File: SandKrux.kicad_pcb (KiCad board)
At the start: 2 copper layers, 69 parts, among them CN1 527450697, J1 FH12-40S-0.5SH_55_, J2 Connector, USB-TYPE-C-16P, U1 K210_C913414, U2 AXP173, U3 MT9700-N, U4 SGM809-ZXN3L/TR, U4 XC6206P182MR_C347373, U5 GD25LQ128EWIGR, U6 TMI7003C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

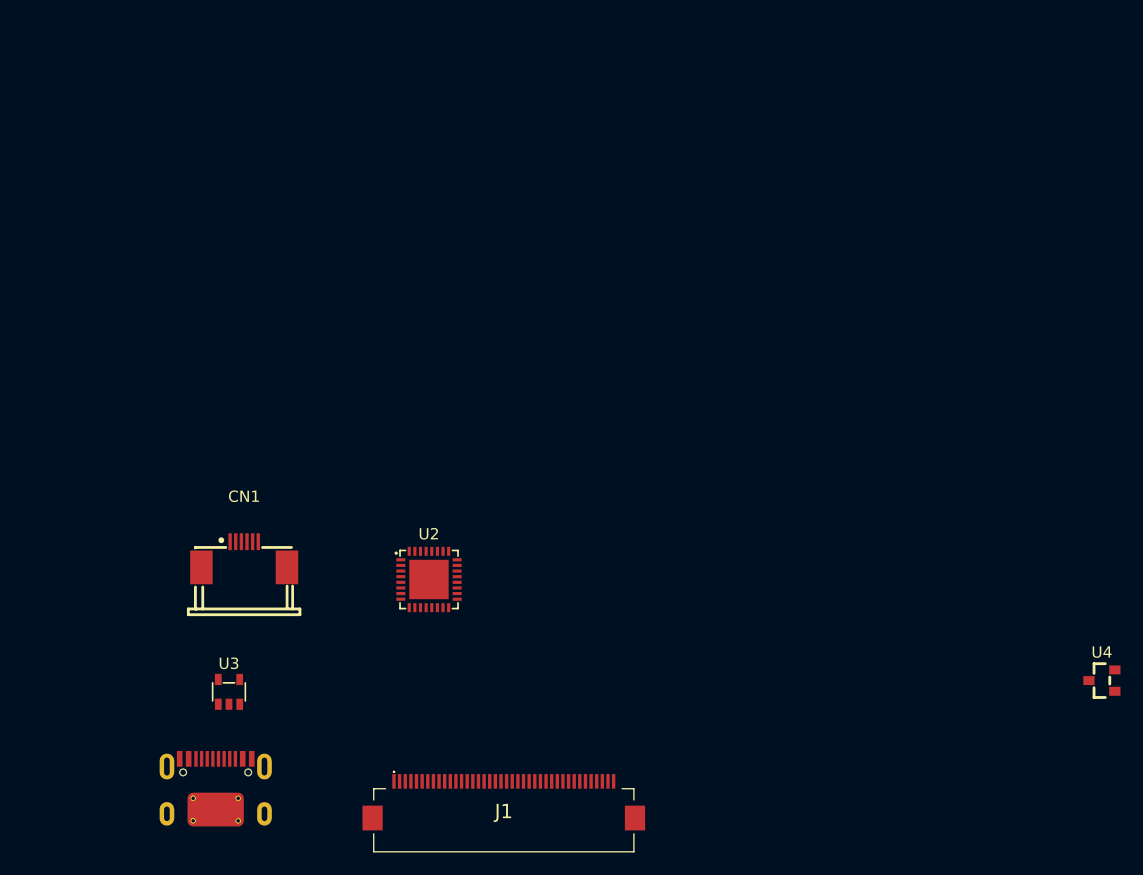
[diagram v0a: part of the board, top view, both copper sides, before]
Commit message: pcb update lcd e toutch
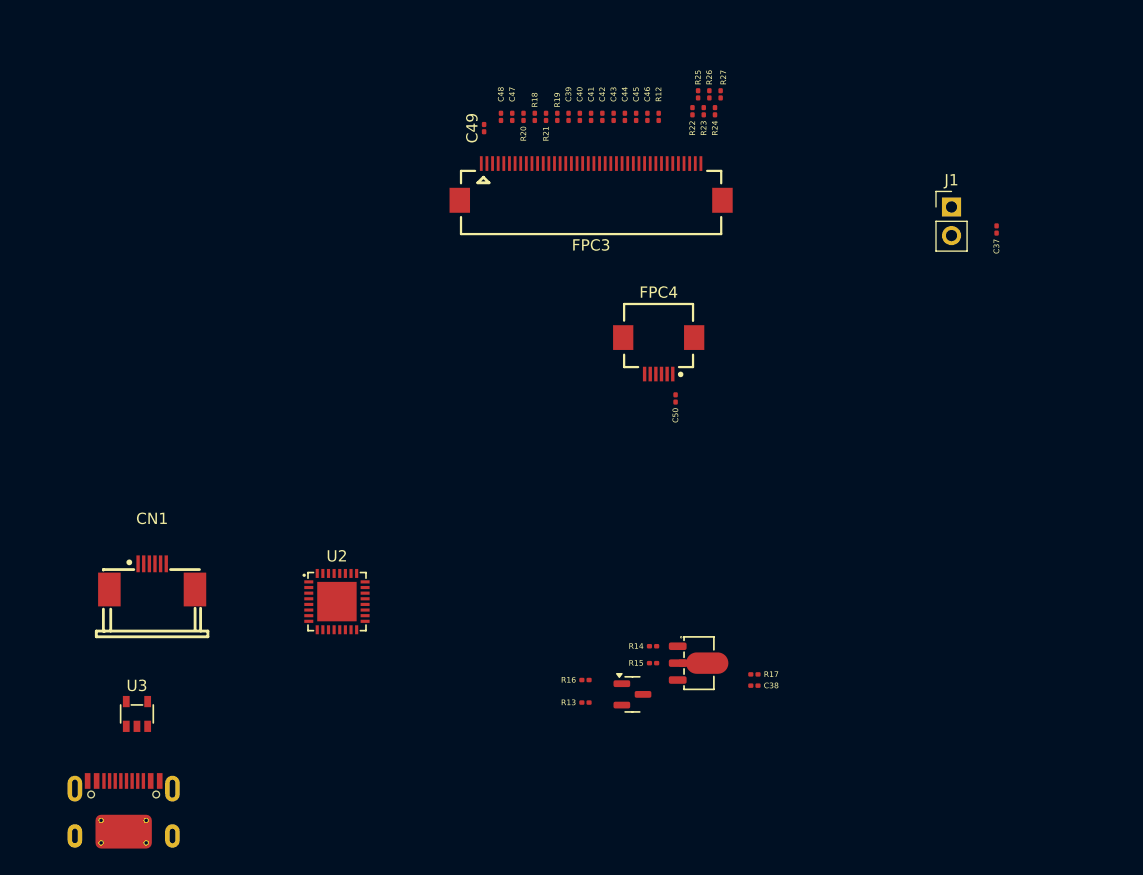
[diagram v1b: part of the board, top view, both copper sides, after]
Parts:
- removed the U4 at (232.8, 90.5)
- added C37: 10uF, Capacitor_SMD:C_0201_0603Metric, F.Cu at (223.5, 50.5)
- added C38: 100nF, Capacitor_SMD:C_0201_0603Metric, F.Cu at (202.0, 91.0)
- added C39: 100pF, Capacitor_SMD:C_0201_0603Metric, F.Cu at (185.5, 40.5)
- added C40: 100pF, Capacitor_SMD:C_0201_0603Metric, F.Cu at (186.5, 40.5)
- added C41: 100pF, Capacitor_SMD:C_0201_0603Metric, F.Cu at (187.5, 40.5)
- added C42: 100pF, Capacitor_SMD:C_0201_0603Metric, F.Cu at (188.5, 40.5)
- added C43: 100pF, Capacitor_SMD:C_0201_0603Metric, F.Cu at (189.5, 40.5)
- added C44: 100pF, Capacitor_SMD:C_0201_0603Metric, F.Cu at (190.5, 40.5)
- added C45: 100pF, Capacitor_SMD:C_0201_0603Metric, F.Cu at (191.5, 40.5)
- added C46: 100pF, Capacitor_SMD:C_0201_0603Metric, F.Cu at (192.5, 40.5)
- added C47: 100pF, Capacitor_SMD:C_0201_0603Metric, F.Cu at (180.5, 40.5)
- added C48: 100pF, Capacitor_SMD:C_0201_0603Metric, F.Cu at (179.5, 40.5)
- added C49: 100nF, Capacitor_SMD:C_0201_0603Metric, F.Cu at (178.0, 41.5)
- added C50: 10uF, Capacitor_SMD:C_0201_0603Metric, F.Cu at (195.0, 65.5)
- added FPC3: FH12-40S-0.5SH(55), easyeda2kicad:FPC-SMD_FH12-40S-0.5SH-55, F.Cu at (187.5, 46.3)
- added FPC4: FH12-6S-0.5SH(55), easyeda2kicad:FPC-SMD_FH12-6S-0.5SH-55, F.Cu at (193.5, 61.7)
- added Q1: S8050, PCM_JLCPCB:Q_SOT-23, F.Cu at (191.2, 91.8)
- added Q2: SI2301CDS-T1-GE3, PCM_JLCPCB:Q_SOT-89, F.Cu at (196.5, 89.0)
- added R12: 5.1R, Resistor_SMD:R_0201_0603Metric, F.Cu at (193.5, 40.5)
- added R13: 100R, Resistor_SMD:R_0201_0603Metric, F.Cu at (187.0, 92.5)
- added R14: 100R, Resistor_SMD:R_0201_0603Metric, F.Cu at (193.0, 87.5)
- added R15: 10K, Resistor_SMD:R_0201_0603Metric, F.Cu at (193.0, 89.0)
- added R16: 10K, Resistor_SMD:R_0201_0603Metric, F.Cu at (187.0, 90.5)
- added R17: 10K, Resistor_SMD:R_0201_0603Metric, F.Cu at (202.0, 90.0)
- added R18: 0R, Resistor_SMD:R_0201_0603Metric, F.Cu at (182.5, 40.5)
- added R19: NC, Resistor_SMD:R_0201_0603Metric, F.Cu at (184.5, 40.5)
- added R20: NC, Resistor_SMD:R_0201_0603Metric, F.Cu at (181.5, 40.5)
- added R21: 0R, Resistor_SMD:R_0201_0603Metric, F.Cu at (183.5, 40.5)
- added R22: NC, Resistor_SMD:R_0201_0603Metric, F.Cu at (196.5, 40.0)
- added R23: NC, Resistor_SMD:R_0201_0603Metric, F.Cu at (197.5, 40.0)
- added R24: 5.1K, Resistor_SMD:R_0201_0603Metric, F.Cu at (198.5, 40.0)
- added R25: 5.1K, Resistor_SMD:R_0201_0603Metric, F.Cu at (197.0, 38.5)
- added R26: 5.1K, Resistor_SMD:R_0201_0603Metric, F.Cu at (198.0, 38.5)
- added R27: NC, Resistor_SMD:R_0201_0603Metric, F.Cu at (199.0, 38.5)
- J1: value FH12-40S-0.5SH_55_ -> Conn_01x02; footprint KiCad:FH1240S05SH55 -> Connector_PinHeader_2.54mm:PinHeader_1x02_P2.54mm_Vertical
- moved J1 66.8 mm to (219.5, 48.5)
- moved CN1 8.40 mm to (148.5, 81.3)
- moved J2 8.40 mm to (146.0, 102.0)
- moved U3 8.40 mm to (147.2, 93.5)
- moved U2 8.40 mm to (164.9, 83.5)
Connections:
- J1 pad 1: unconnected-(J1-Pad1) -> /CAPTOUCH_RST
- J1 pad 2: unconnected-(J1-Pad2) -> /FUNCTION2

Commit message: TFT CARD
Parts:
- added C51: 10uF, Capacitor_SMD:C_0201_0603Metric, F.Cu at (36.0, 61.0)
- added R28: 10K, Resistor_SMD:R_0201_0603Metric, F.Cu at (35.0, 61.0)
- added R29: 10K, Resistor_SMD:R_0201_0603Metric, F.Cu at (39.5, 61.0)
- added U9: HX TF-CARD XG8P H1.5, easyeda2kicad:TF-SMD_HX-TF-CARD-XG8P-H1.5, F.Cu at (36.2, 67.4)

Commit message: usb ports
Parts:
- removed J2: Connector, USB-TYPE-C-16P, PCM_JLCPCB:TYPE-C-SMD_HX-TYPE-C-16PIN
- added R30: 5.1K, Resistor_SMD:R_0201_0603Metric, F.Cu at (81.0, 126.5)
- added R31: 5.1K, Resistor_SMD:R_0201_0603Metric, F.Cu at (84.5, 126.5)
- added R32: 1.5K, Resistor_SMD:R_0201_0603Metric, F.Cu at (63.8, 117.4)
- added R33: 1.5K, Resistor_SMD:R_0201_0603Metric, F.Cu at (63.8, 119.2)
- added R34: 1.5K, Resistor_SMD:R_0201_0603Metric, F.Cu at (66.2, 113.9)
- added R35: 1.5K, Resistor_SMD:R_0201_0603Metric, F.Cu at (66.2, 115.7)
- added R36: 1.5K, Resistor_SMD:R_0201_0603Metric, F.Cu at (66.2, 117.4)
- added R37: 1.5K, Resistor_SMD:R_0201_0603Metric, F.Cu at (66.2, 119.2)
- added R38: 1.5K, Resistor_SMD:R_0201_0603Metric, F.Cu at (81.5, 105.5)
- added R39: 1.5K, Resistor_SMD:R_0201_0603Metric, F.Cu at (98.5, 105.5)
- added R40: NC, Resistor_SMD:R_0201_0603Metric, F.Cu at (68.7, 117.4)
- added R41: 0R, Resistor_SMD:R_0201_0603Metric, F.Cu at (68.7, 119.2)
- added SW1: TL3330AF130QG, easyeda2kicad:SW-SMD_E-SWITCH_TL3330, F.Cu at (57.9, 105.9)
- added SW2: TL3330AF130QG, easyeda2kicad:SW-SMD_E-SWITCH_TL3330, F.Cu at (57.9, 111.4)
- added SW3: TL3330AF130QG, easyeda2kicad:SW-SMD_E-SWITCH_TL3330, F.Cu at (81.5, 107.5)
- added SW4: TL3330AF130QG, easyeda2kicad:SW-SMD_E-SWITCH_TL3330, F.Cu at (98.5, 107.5)
- added SW5: TL3330AF130QG, easyeda2kicad:SW-SMD_E-SWITCH_TL3330, F.Cu at (57.9, 127.9)
- added USB1: HYCW412-USBC16-065B, easyeda2kicad:USB-C-SMD_HYCW412-USBC16-065B, F.Cu at (82.5, 131.7)

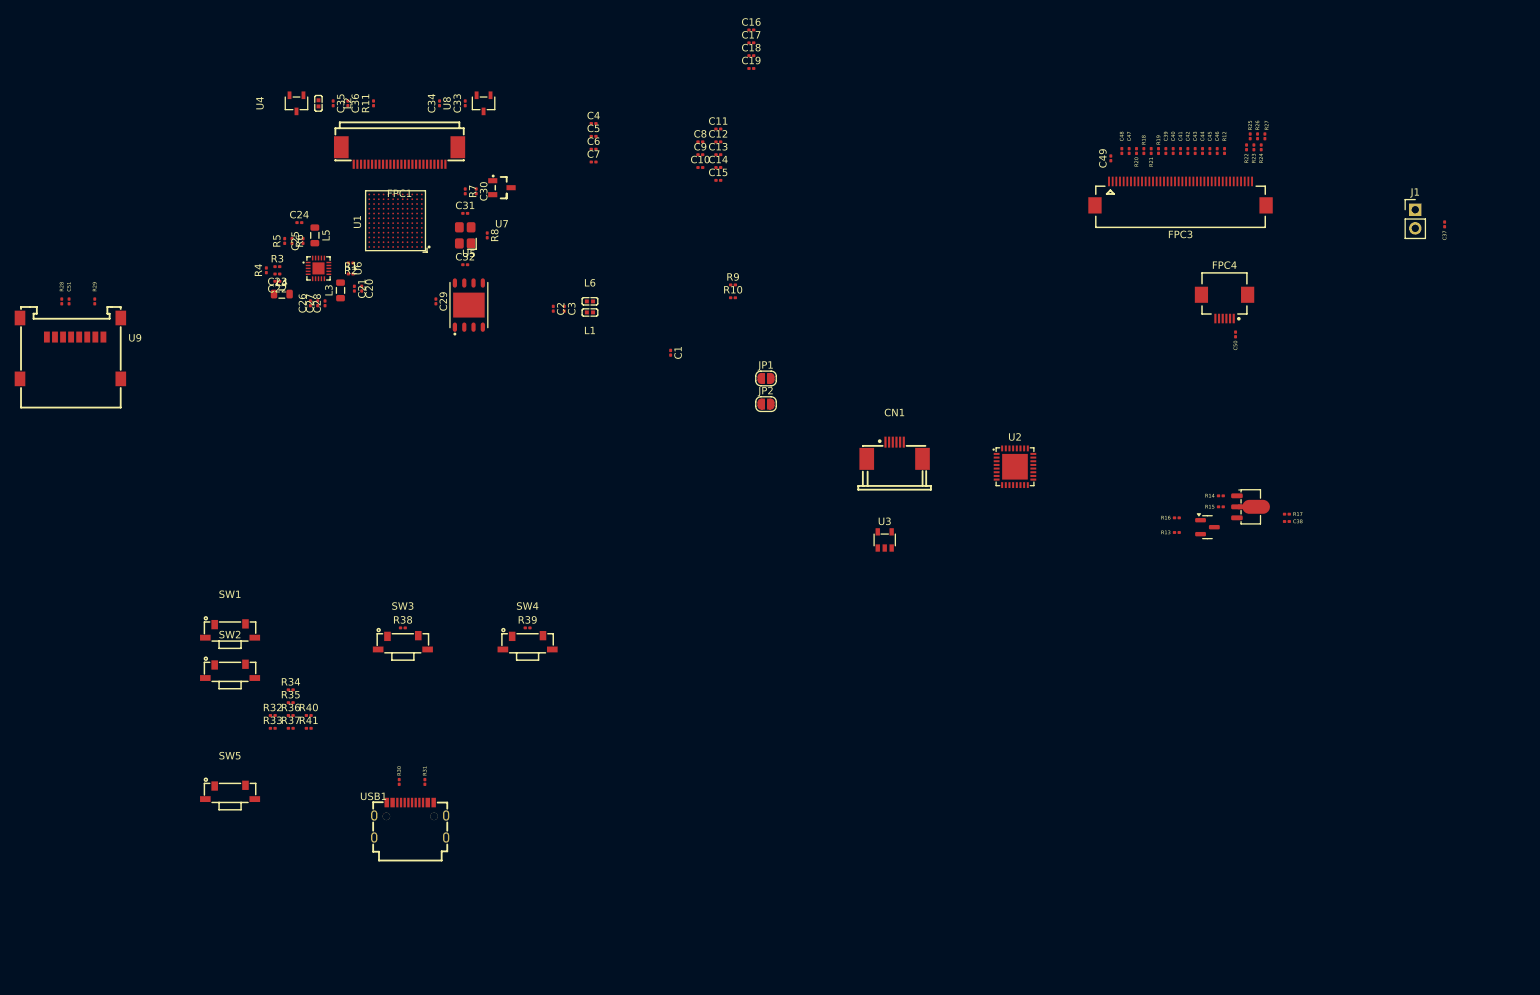
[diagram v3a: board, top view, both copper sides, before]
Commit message: AXP173 batery module
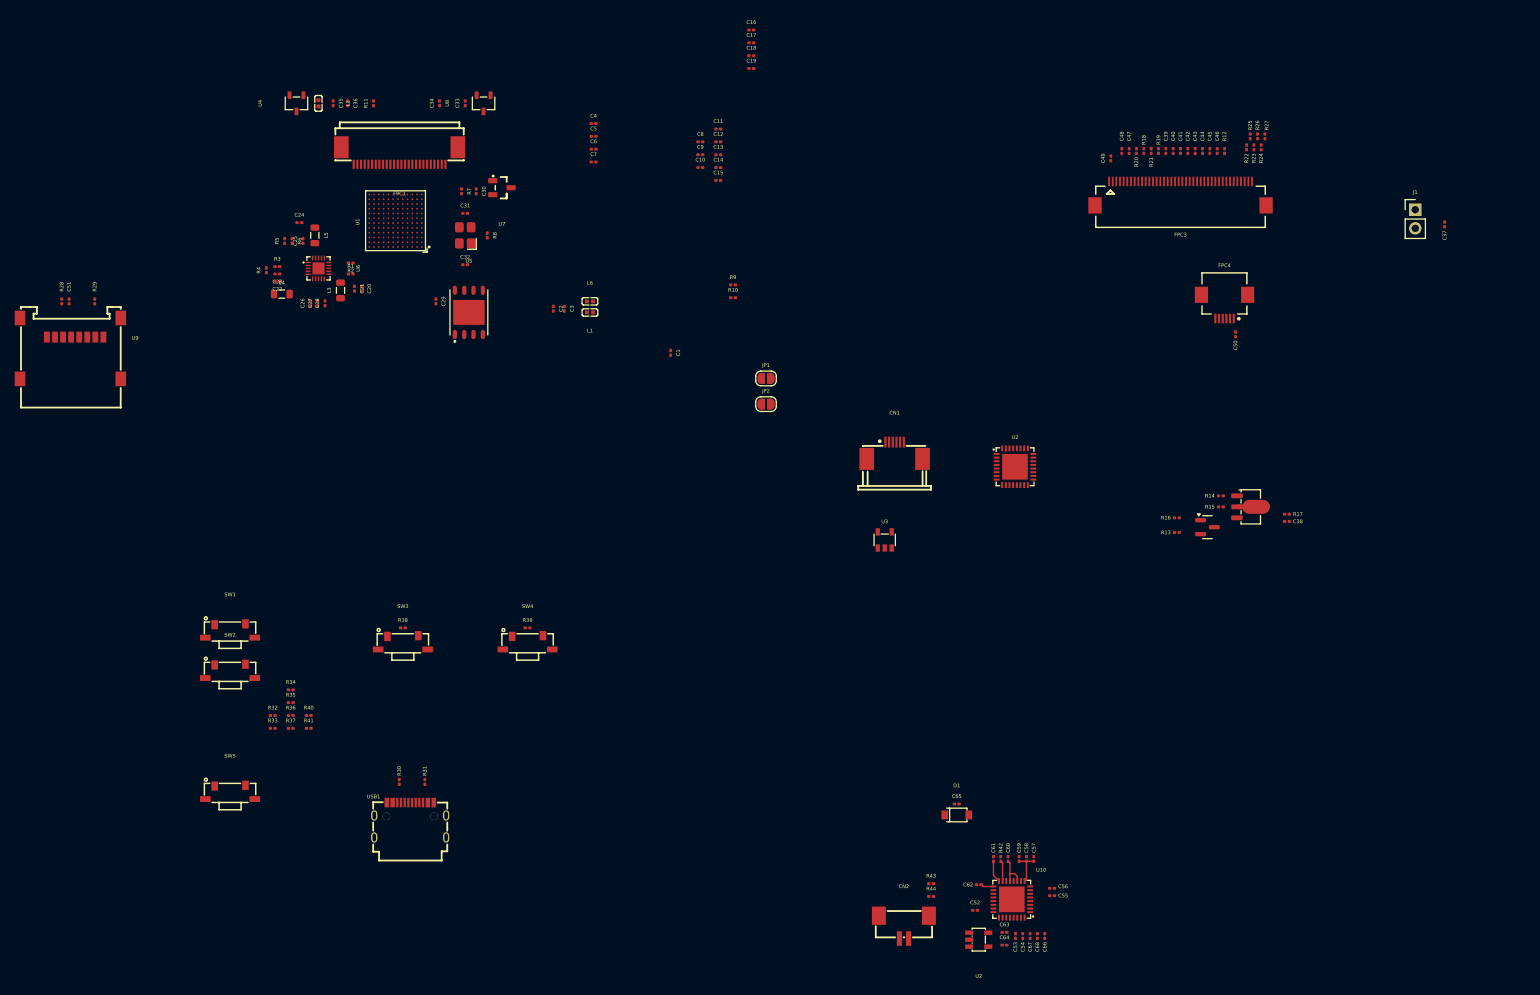
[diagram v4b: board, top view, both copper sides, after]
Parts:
- added C52: 22uF, Capacitor_SMD:C_0201_0603Metric, F.Cu at (159.5, 144.0)
- added C53: 10uF, Capacitor_SMD:C_0201_0603Metric, F.Cu at (165.0, 147.5)
- added C54: 1nF, Capacitor_SMD:C_0201_0603Metric, F.Cu at (166.0, 147.5)
- added C55: 10uF, Capacitor_SMD:C_0201_0603Metric, F.Cu at (170.0, 142.0)
- added C56: 100nF, Capacitor_SMD:C_0201_0603Metric, F.Cu at (170.0, 141.0)
- added C57: 22uF, Capacitor_SMD:C_0201_0603Metric, F.Cu at (167.5, 137.0)
- added C58: 10uF, Capacitor_SMD:C_0201_0603Metric, F.Cu at (166.5, 137.0)
- added C59: 22uF, Capacitor_SMD:C_0201_0603Metric, F.Cu at (165.5, 137.0)
- added C60: 1uF, Capacitor_SMD:C_0201_0603Metric, F.Cu at (164.0, 137.0)
- added C61: 220uF, Capacitor_SMD:C_0201_0603Metric, F.Cu at (162.0, 137.0)
- added C62: 1uF, Capacitor_SMD:C_0201_0603Metric, F.Cu at (160.0, 140.5)
- added C63: 220nF, Capacitor_SMD:C_0201_0603Metric, F.Cu at (163.5, 147.0)
- added C64: 22uF, Capacitor_SMD:C_0201_0603Metric, F.Cu at (163.5, 148.8)
- added C65: 10uF, Capacitor_SMD:C_0201_0603Metric, F.Cu at (157.0, 129.5)
- added C66: 22uF, Capacitor_SMD:C_0201_0603Metric, F.Cu at (169.0, 147.5)
- added C67: 22uF, Capacitor_SMD:C_0201_0603Metric, F.Cu at (167.0, 147.5)
- added C68: 22uF, Capacitor_SMD:C_0201_0603Metric, F.Cu at (168.0, 147.5)
- added CN2: 1.25mm-2P socket, easyeda2kicad:CONN-SMD_1.25T-2P, F.Cu at (149.8, 146.3)
- added D1: 1N5819HW-7-F, easyeda2kicad:SOD-123_L2.7-W1.6-LS3.7-RD, F.Cu at (157.0, 131.0)
- added R42: 200K, Resistor_SMD:R_0201_0603Metric, F.Cu at (163.0, 137.0)
- added R43: 0R, Resistor_SMD:R_0201_0603Metric, F.Cu at (153.5, 140.4)
- added R44: 10K, Resistor_SMD:R_0201_0603Metric, F.Cu at (153.5, 142.1)
- added U10: AXP173_C3345106, easyeda2kicad:QFN-32_L5.0-W5.0-P0.50-TL-EP3.5-1, F.Cu at (164.5, 142.5)
- added U2: MT9700, easyeda2kicad:SOT-23-5_L3.0-W1.7-P0.95-LS2.8-BR, F.Cu at (160.0, 148.0)
- moved U5 1.00 mm to (90.5, 62.5)
- moved R7 0.50 mm to (89.5, 46.0)
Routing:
- net /ADD_3V0: track 0.00 -> 4.78 mm
- net /IPSOUT: track 0.00 -> 4.57 mm
- net Net-(U10-VREF): track 0.00 -> 2.99 mm
- net Net-(U10-BIAS): track 0.00 -> 2.78 mm
- net Net-(U10-VINT): track 0.00 -> 1.78 mm
